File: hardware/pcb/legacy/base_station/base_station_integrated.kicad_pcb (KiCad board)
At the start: 2 copper layers, 171.4 x 127 mm, 400 parts, among them CON1 RJ45_TART, CON2 RJ45_TART, CON3 RJ45_TART, CON4 RJ45_TART, CON5 RJ45_TART, CON6 RJ45_TART, CON7 RJ45_TART, CON8 RJ45_TART, IC1 LTC2851, IC10 LTC2851, IC11 LTC2851, IC12 LTC2851, IC13 LTC2851, IC14 LTC2851, IC15 LTC2851, IC16 LTC2851, IC17 LTC2851, IC18 LTC2851, IC19 LTC2851, IC2 LTC2851, IC20 LTC2851, IC21 LTC2851, IC22 LTC2851, IC23 LTC2851, IC24 LTC2851, IC26 XTAL_DRIVER_TART, IC3 LTC2851, IC4 LTC2851, IC5 LTC2851, IC6 LTC2851, IC7 LTC2851, IC8 LTC2851, IC9 LTC2851, P1 CONN_20X2, SW1 SWITCH, U1 PAPILIO_TART, U2 BMIS-105_BMIS-205, X1 TCXO_TART

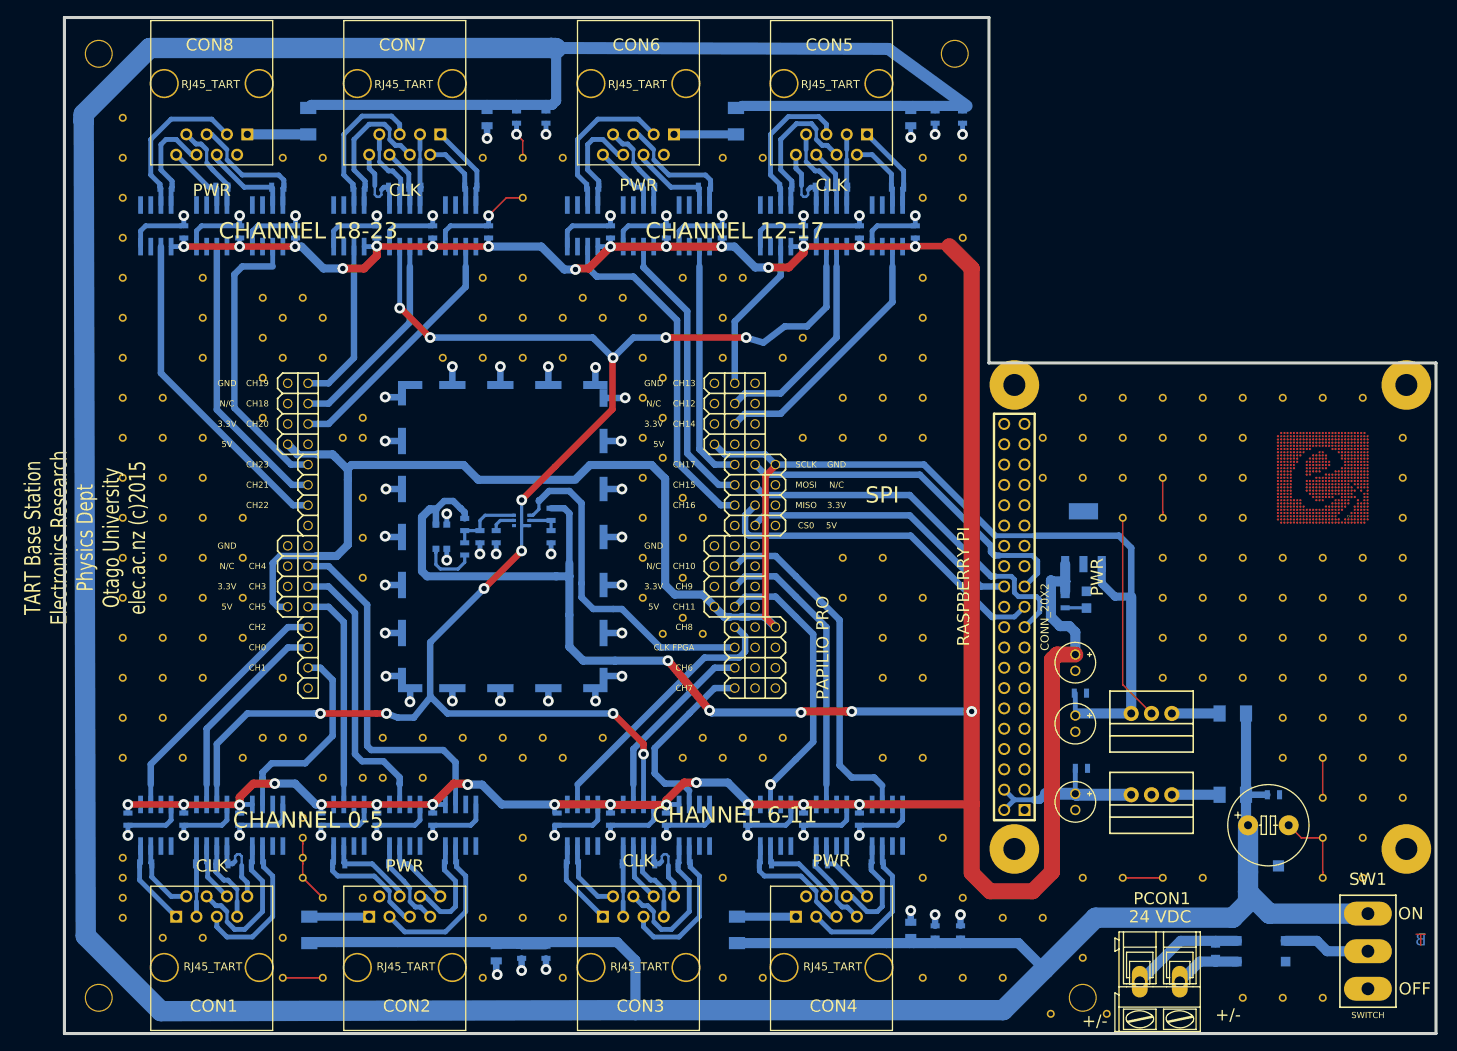
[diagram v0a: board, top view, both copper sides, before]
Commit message: Moved things around so that old files are in the legacy directory
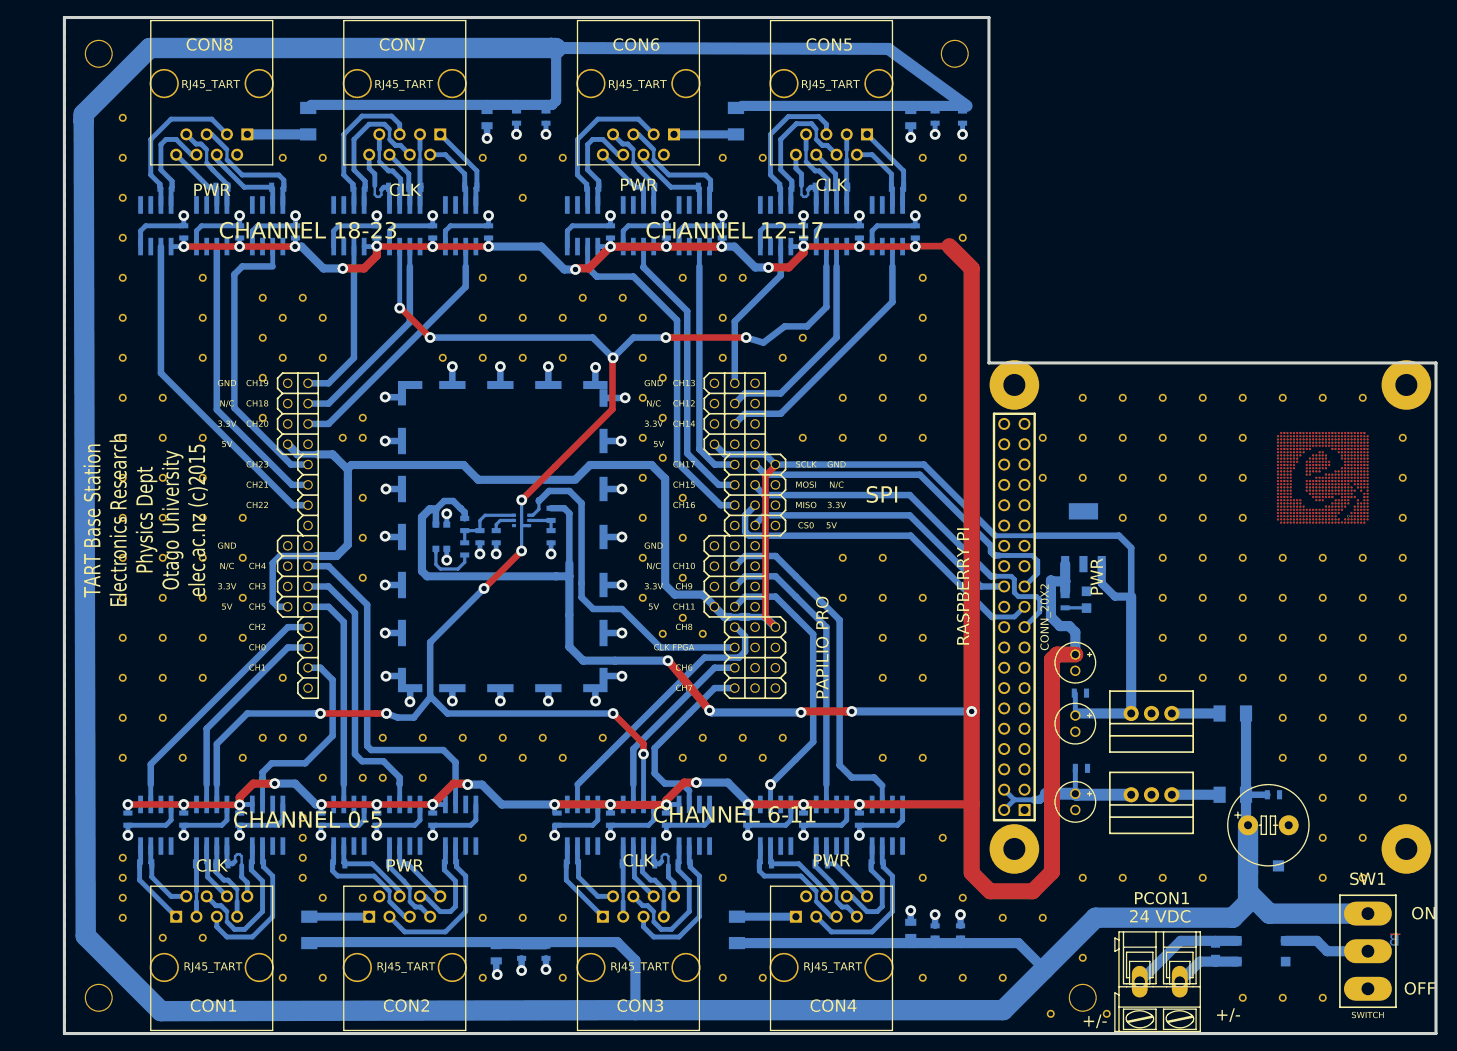
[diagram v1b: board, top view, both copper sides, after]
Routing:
- net GND: track 357.9 -> 285.1 mm
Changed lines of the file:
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@@
     (thickness 1.6002)
     (drawings 77)
-    (tracks 1373)
+    (tracks 1352)
     (zones 0)
     (modules 400)
@@
     (solder_mask_min_width 0.25)
     (aux_axis_origin 52.705 164.465)
-    (visible_elements 7FF9FFFF)
+    (visible_elements 7FFFFFFF)
     (pcbplotparams
-      (layerselection 0x00030_ffffffff)
+      (layerselection 0x00030_80000001)
       (usegerberextensions true)
       (usegerberattributes false)
@@
       (drillshape 0)
       (scaleselection 1)
-      (outputdirectory "/home/phillb/TART/hardware/pcb/kicad/base_int_eng/"))
+      (outputdirectory "../../../../freenas/eagle_files/tart/TART2_a/base_station_integrated/"))
   )
   (net 0 "")
@@
     (fp_line (start 3.5 -7) (end 3.5 7) (layer F.SilkS) (width 0.2032))
     (fp_line (start -3.5 -7) (end -3.5 7) (layer F.SilkS) (width 0.2032))
-    (fp_text user OFF (at 5.854 4.7) (layer F.SilkS)
+    (fp_text user OFF (at 6.5 4.7) (layer F.SilkS)
       (effects (font (size 1.524 1.524) (thickness 0.3048)))
     )
-    (fp_text user ON (at 5.354 -4.7) (layer F.SilkS)
+    (fp_text user ON (at 7 -4.7) (layer F.SilkS)
       (effects (font (size 1.524 1.524) (thickness 0.3048)))
     )
@@
     (effects (font (size 1.524 1.524) (thickness 0.3048)))
   )
-  (gr_text "TART Base Station \nElectronics Research\nPhysics Dept\nOtago University\nelec.ac.nz (c)2015" (at 55.3 102.5 90) (layer F.SilkS)
+  (gr_text "TART Base Station \nElectronics Research\nPhysics Dept\nOtago University\nelec.ac.nz (c)2015" (at 62.8 100.3 90) (layer F.SilkS)
     (effects (font (size 2.032 1.524) (thickness 0.3048)))
   )
@@
     (effects (font (size 1.524 1.524) (thickness 0.3048)))
   )
-  (gr_text B (at 222.25 152.75) (layer Back)
+  (gr_text B (at 218.948 152.781) (layer Back)
     (effects (font (size 1.524 1.524) (thickness 0.3048)) (justify mirror))
   )
-  (gr_text T (at 222.25 152.781) (layer Front)
+  (gr_text T (at 219.075 152.781) (layer Front)
     (effects (font (size 1.524 1.524) (thickness 0.3048)))
   )
@@
   (segment (start 67.6275 62.23) (end 67.6275 63.5) (width 0.6096) (layer Back) (net 35) (status 20))
   (via (at 91.7575 62.23) (size 1.35) (layers Front Back) (net 35))
-  (segment (start 107.9575 60) (end 110 60) (width 0.2032) (layer Front) (net 35))
-  (segment (start 105.7275 62.23) (end 107.9575 60) (width 0.2032) (layer Front) (net 35))
-  (segment (start 110 52.85) (end 109.22 52.07) (width 0.2032) (layer Front) (net 35))
-  (segment (start 110 55) (end 110 52.85) (width 0.2032) (layer Front) (net 35))
-  (segment (start 82.5 140.707106) (end 82.5 142.5) (width 0.2032) (layer Front) (net 35))
-  (segment (start 82.5 140) (end 82.5 140.707106) (width 0.2032) (layer Front) (net 35))
-  (segment (start 82.5 143.207106) (end 82.5 145) (width 0.2032) (layer Front) (net 35))
-  (segment (start 82.5 142.5) (end 82.5 143.207106) (width 0.2032) (layer Front) (net 35))
-  (segment (start 82.5 145) (end 85 147.5) (width 0.2032) (layer Front) (net 35))
-  (segment (start 80 157.5) (end 85 157.5) (width 0.2032) (layer Front) (net 35))
-  (segment (start 185.707106 145) (end 190 145) (width 0.2032) (layer Front) (net 35))
-  (segment (start 185 145) (end 185.707106 145) (width 0.2032) (layer Front) (net 35))
-  (segment (start 210 144.292894) (end 210 140) (width 0.2032) (layer Front) (net 35))
-  (segment (start 210 145) (end 210 144.292894) (width 0.2032) (layer Front) (net 35))
-  (segment (start 207.31 140) (end 205.74 138.43) (width 0.2032) (layer Front) (net 35))
-  (segment (start 210 140) (end 207.31 140) (width 0.2032) (layer Front) (net 35))
-  (segment (start 210 135) (end 210 130) (width 0.2032) (layer Front) (net 35))
-  (segment (start 190 99.292894) (end 190 95) (width 0.2032) (layer Front) (net 35))
-  (segment (start 190 100) (end 190 99.292894) (width 0.2032) (layer Front) (net 35))
-  (segment (start 185 120.865) (end 188.595 124.46) (width 0.2032) (layer Front) (net 35))
-  (segment (start 185 100) (end 185 120.865) (width 0.2032) (layer Front) (net 35))
   (segment (start 97.155 60.90158) (end 97.155 58.801) (width 0.6096) (layer Back) (net 36) (status 30))
   (segment (start 97.155 55.245) (end 97.155 58.547) (width 0.6096) (layer Back) (net 36) (status 20))
